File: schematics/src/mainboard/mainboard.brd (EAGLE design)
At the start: 43.2 x 99.1 mm, 64 parts, among them IC1 CEM3340, IC2 TL074P, IC4 TL074P, Q1 2N3904, Q2 2N3904

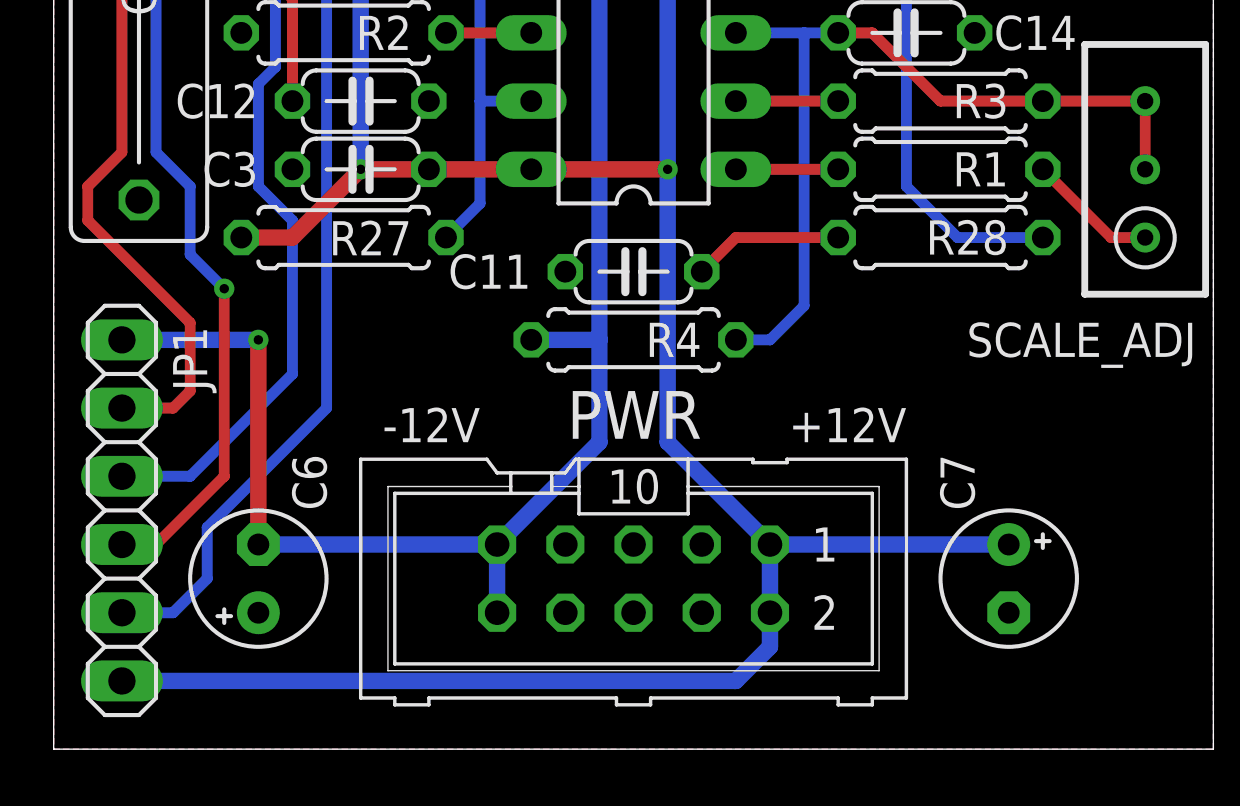
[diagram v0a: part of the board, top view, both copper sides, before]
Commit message: Updated Schematics, Fixed Power Socket orientation
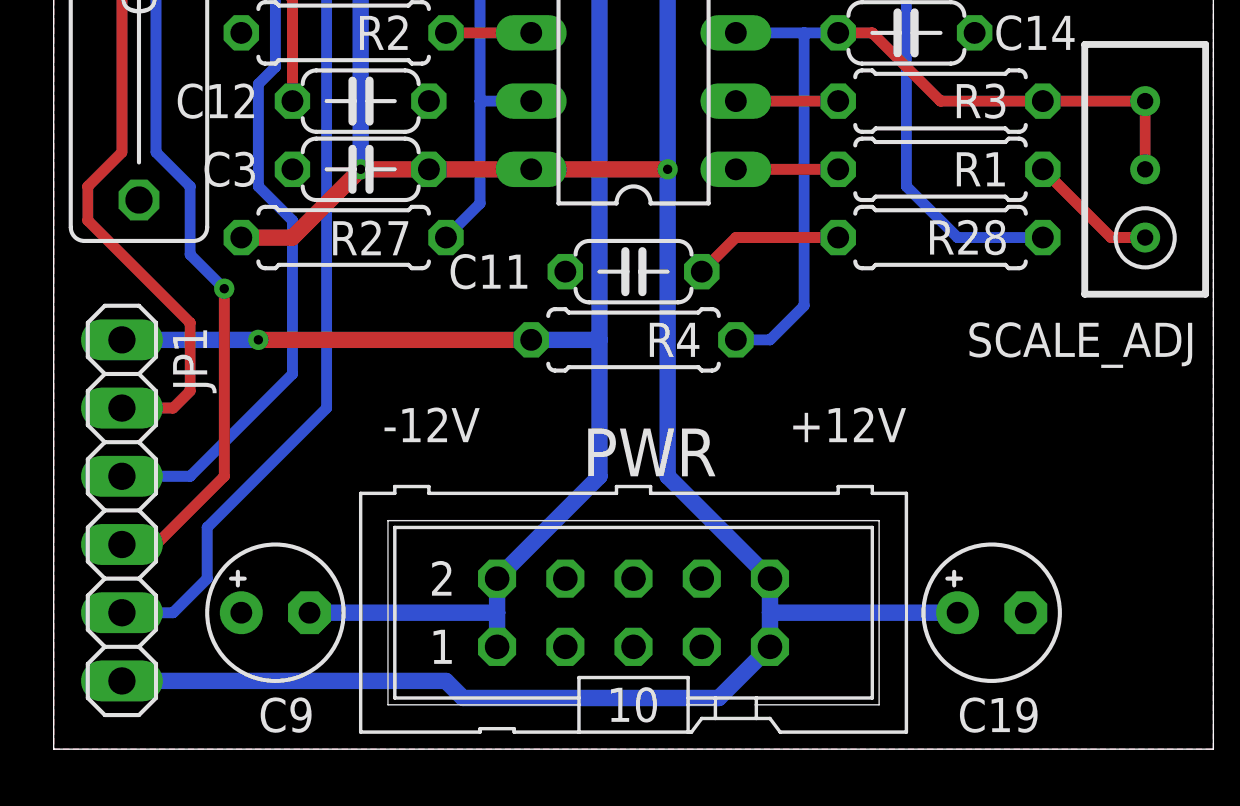
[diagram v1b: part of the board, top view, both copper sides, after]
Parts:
- removed C6, C7: 10uf, resistor:E2,5-5
- added C19, C9: 10uf, resistor:E2,5-5
- moved PWR 1.27 mm to (21.6, 5.08), turned to 0 degrees
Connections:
- net +12V: now also C19.+, PWR.10, PWR.9; no longer C7.+, PWR.1, PWR.2
- net -12V: now also C9.-, PWR.1, PWR.2; no longer C6.-, PWR.10, PWR.9
- net GND: now also C19.-, C9.+; no longer C6.+, C7.-
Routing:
- net -12V: track 134.6 -> 136.5 mm
- net +12V: track 174.7 -> 173.3 mm

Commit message: Fixed issues
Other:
- board text added: "CURTIS 3340 VCO v1.2 GERBSTER.NL 2022"
- board text removed: "CURTIS 3340 VCO v1.1 GERBSTER.NL 2020"
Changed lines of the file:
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@@
 <wire x1="0" y1="99.06" x2="0" y2="0" width="0" layer="20"/>
 <wire x1="0" y1="0" x2="43.18" y2="0" width="0" layer="20"/>
-<text x="42.545" y="76.2" size="1.4224" layer="25" font="vector" rot="R90">CURTIS 3340 VCO v1.1
-GERBSTER.NL 2020</text>
+<text x="42.545" y="76.2" size="1.4224" layer="25" font="vector" rot="R90">CURTIS 3340 VCO v1.2
+GERBSTER.NL 2022</text>
 <text x="15.875" y="12.7" size="1.27" layer="25" font="vector" rot="R180">-12V</text>
 <text x="31.75" y="12.7" size="1.27" layer="25" font="vector" rot="R180">+12V</text>
